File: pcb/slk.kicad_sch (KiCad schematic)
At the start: 10 parts, among them J1 Screw Terminal, P1 Power, P2 Analog, P3 Digital 1, P4 Digital 2, U1 MCP2515-xSO, Y1 Crystal

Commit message: finished schema
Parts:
- added U2: TJA1055T1, symbol Symbols:TJA1055T
- C1, C2: value C -> 22pF
- R1: value R -> 10K
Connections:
- net 5V: now also U2.10 (VCC)
- net GND: now also U2.13 (GND)
- net BAT+: now reaches J1.1 (Pin_1)
- net BAT+: now also U2.14 (BAT)
- net CANL: now reaches J1.2 (Pin_2)
- net CANL: now also U2.12 (CANL)
- net CANH: now reaches J1.3 (Pin_3)
- net CANH: now also U2.11 (CANH)
- net TX: now reaches U1.1 (TXCAN)
- net TX: now also U2.2 (TXD)
- net RX: now reaches U1.2 (RXCAN)
- net RX: now also U2.3 (RXD)
- new net EN: U2.6 (EN)
- new net ERR: U2.4 (ERR)
- new net INH: U2.1 (INH)
- new net STB: U2.5 (STB)
- new net WAKE: U2.7 (WAKE)
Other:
- moved on the sheet: J1

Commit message: add footprints
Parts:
- C1, C2: footprint (none) -> Capacitor_SMD:C_0402_1005Metric
- J1: footprint (none) -> TerminalBlock:TerminalBlock_bornier-3_P5.08mm
- P1, P3: footprint (none) -> Connector_PinHeader_2.54mm:PinHeader_1x08_P2.54mm_Vertical
- P2: footprint (none) -> Connector_PinHeader_2.54mm:PinHeader_1x06_P2.54mm_Vertical
- P4: footprint (none) -> Connector_PinHeader_2.54mm:PinHeader_1x10_P2.54mm_Vertical
- R1: footprint (none) -> Resistor_SMD:R_0402_1005Metric
- U2: footprint (none) -> Package_SO:SOIC-14_3.9x8.7mm_P1.27mm
- Y1: footprint (none) -> Crystal:Crystal_SMD_ECS_CSM3X-2Pin_7.6x4.1mm
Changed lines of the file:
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@@
 			)
 		)
-		(property "Footprint" ""
+		(property "Footprint" "Resistor_SMD:R_0402_1005Metric"
 			(at 139.7 122.428 90)
 			(effects
@@
 			)
 		)
-		(property "Footprint" ""
+		(property "Footprint" "TerminalBlock:TerminalBlock_bornier-3_P5.08mm"
 			(at 219.71 95.25 0)
 			(effects
@@
 			)
 		)
-		(property "Footprint" ""
+		(property "Footprint" "Connector_PinHeader_2.54mm:PinHeader_1x08_P2.54mm_Vertical"
 			(at 31.75 33.02 0)
 			(effects
@@
 			)
 		)
-		(property "Footprint" ""
+		(property "Footprint" "Connector_PinHeader_2.54mm:PinHeader_1x06_P2.54mm_Vertical"
 			(at 31.75 58.42 0)
 			(effects
@@
 			)
 		)
-		(property "Footprint" ""
+		(property "Footprint" "Connector_PinHeader_2.54mm:PinHeader_1x10_P2.54mm_Vertical"
 			(at 49.53 38.1 0)
 			(effects
@@
 			)
 		)
-		(property "Footprint" ""
+		(property "Footprint" "Capacitor_SMD:C_0402_1005Metric"
 			(at 94.9452 147.32 0)
 			(effects
@@
 			)
 		)
-		(property "Footprint" ""
+		(property "Footprint" "Crystal:Crystal_SMD_ECS_CSM3X-2Pin_7.6x4.1mm"
 			(at 90.17 134.62 0)
 			(effects
@@
 			)
 		)
-		(property "Footprint" ""
+		(property "Footprint" "Capacitor_SMD:C_0402_1005Metric"
 			(at 87.3252 147.32 0)
 			(effects
@@
 			)
 		)
-		(property "Footprint" ""
+		(property "Footprint" "Connector_PinHeader_2.54mm:PinHeader_1x08_P2.54mm_Vertical"
 			(at 49.53 63.5 0)
 			(effects
@@
 			)
 		)
-		(property "Footprint" ""
+		(property "Footprint" "Package_SO:SOIC-14_3.9x8.7mm_P1.27mm"
 			(at 162.56 87.63 0)
 			(effects

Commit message: draw board outline
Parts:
- added H1, H2, H3, H4: MountingHole, MountingHole:MountingHole_3.2mm_M3, symbol Mechanical:MountingHole

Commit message: it should work now
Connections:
- net EN: now also P3.7 (Pin_7)
- net ERR: now also P3.5 (Pin_5)
- net INH: now also P3.4 (Pin_4)
- net STB: now also P3.6 (Pin_6)
- net WAKE: now also P3.8 (Pin_8)
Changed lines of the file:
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@@
+	(wire
+		(pts
+			(xy 58.42 63.5) (xy 54.61 63.5)
+		)
+		(stroke
+			(width 0)
+			(type default)
+		)
+	)
+	(wire
+		(pts
+			(xy 58.42 58.42) (xy 54.61 58.42)
+		)
+		(stroke
+			(width 0)
+			(type default)
+		)
+	)
 	(wire
 		(pts
@@
 	(wire
 		(pts
+			(xy 58.42 55.88) (xy 54.61 55.88)
+		)
+		(stroke
+			(width 0)
+			(type default)
+		)
+	)
+	(wire
+		(pts
 			(xy 187.96 97.79) (xy 214.63 97.79)
 		)
@@
 	(wire
 		(pts
+			(xy 58.42 60.96) (xy 54.61 60.96)
+		)
+		(stroke
+			(width 0)
+			(type default)
+		)
+	)
+	(wire
+		(pts
 			(xy 190.5 92.71) (xy 187.96 92.71)
 		)
@@
 		(pts
 			(xy 116.84 81.28) (xy 116.84 85.09)
+		)
+		(stroke
+			(width 0)
+			(type default)
+		)
+	)
+	(wire
+		(pts
+			(xy 58.42 53.34) (xy 54.61 53.34)
 		)
 		(stroke
@@
 		)
 	)
+	(label "ERR"
+		(at 58.42 60.96 0)
+		(fields_autoplaced yes)
+		(effects
+			(font
+				(size 1.27 1.27)
+			)
+			(justify left bottom)
+		)
+	)
 	(label "CS"
 		(at 58.42 43.18 0)
@@
 		)
 	)
+	(label "INH"
+		(at 58.42 63.5 0)
+		(fields_autoplaced yes)
+		(effects
+			(font
+				(size 1.27 1.27)
+			)
+			(justify left bottom)
+		)
+	)
 	(label "SCK"
 		(at 58.42 35.56 0)
@@
 		)
 	)
+	(label "WAKE"
+		(at 58.42 53.34 0)
+		(fields_autoplaced yes)
+		(effects
+			(font
+				(size 1.27 1.27)
+			)
+			(justify left bottom)
+		)
+	)
 	(label "SCK"
 		(at 96.52 97.79 0)
@@
 		)
 	)
+	(label "STB"
+		(at 58.42 58.42 0)
+		(fields_autoplaced yes)
+		(effects
+			(font
+				(size 1.27 1.27)
+			)
+			(justify left bottom)
+		)
+	)
 	(label "CANL"
 		(at 190.5 95.25 0)
@@
 		(fields_autoplaced yes)
 		(effects
+			(font
+				(size 1.27 1.27)
+			)
+			(justify left bottom)
+		)
+	)
+	(label "EN"
+		(at 58.42 55.88 0)
+		(fields_autoplaced yes)
+		(effects

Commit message: leds
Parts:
- added D1: ERR, LED_SMD:LED_0603_1608Metric, symbol Device:LED
- added D2: RX, LED_SMD:LED_0603_1608Metric, symbol Device:LED
- added D3: TX, LED_SMD:LED_0603_1608Metric, symbol Device:LED
- added R1, R2, R3: R, Resistor_SMD:R_0402_1005Metric, symbol Device:R
- added SW1: SW_SPDT, Button_Switch_SMD:SW_SPDT_CK_JS102011SAQN, symbol Switch:SW_SPDT
- Y1: value Crystal -> 16MHz
- renumbered R1 to R4
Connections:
- net 5V: now also R1.2, SW1.3 (C)
- net BAT+: now also J1.3 (Pin_3), SW1.1 (A); no longer J1.1 (Pin_1), U2.14 (BAT)
- net CANH: now also J1.1 (Pin_1); no longer J1.3 (Pin_3)
- net ERR: now also D1.1 (K)
- net GND: now also D2.1 (K), D3.1 (K)
- net RX: now also R2.2
- net TX: now also R3.2
- new net: D3.2 (A), R3.1
- new net: D2.2 (A), R2.1
- new net: D1.2 (A), R1.1
- new net: SW1.2 (B), U2.14 (BAT)

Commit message: done
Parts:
- C1, C2: Part Number (none) -> GRM1555C1H220JA01D
- D1: Part Number (none) -> LTST-C190GKT
- D2: Part Number (none) -> LTST-C191KRKT
- D3: Part Number (none) -> LTST-C193TBKT-5A
- J1: Part Number (none) -> TERM BLK 3P SIDE ENT 5.08MM PCB
- P1, P3: Part Number (none) -> 200-SSW10803GS
- P2: Part Number (none) -> 200-SSW10603GS
- P4: Part Number (none) -> 200-SSW11003GS
- R1, R2, R3: value R -> 330; Part Number (none) -> RC0402JR-07330RL
- R4: Part Number (none) -> RC0402JR-0710KL
- SW1: Part Number (none) -> JS102011SAQN
- U1: Part Number (none) -> MCP2515T-I/SO
- U2: Part Number (none) -> TJA1055T/1J (935302723118)
- Y1: Part Number (none) -> ECS-160-20-3X-TR
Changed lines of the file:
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@@
+			)
+		)
+		(property "Part Number" "RC0402JR-0710KL"
+			(at 139.7 120.65 0)
+			(effects
+				(font
+					(size 1.27 1.27)
+				)
+				(hide yes)
 			)
 		)
@@
 			)
 		)
+		(property "Part Number" "TERM BLK 3P SIDE ENT 5.08MM PCB"
+			(at 219.71 95.25 0)
+			(effects
+				(font
+					(size 1.27 1.27)
+				)
+				(hide yes)
+			)
+		)
 		(pin "2"
 		)
@@
 			)
 		)
+		(property "Part Number" "200-SSW10803GS"
+			(at 31.75 33.02 0)
+			(effects
+				(font
+					(size 1.27 1.27)
+				)
+				(hide yes)
+			)
+		)
 		(pin "1"
 		)
@@
 			)
 		)
+		(property "Part Number" ""
+			(at 127 25.4 0)
+			(effects
+				(font
+					(size 1.27 1.27)
+				)
+				(hide yes)
+			)
+		)
 		(instances
 			(project "slk"
@@
 		)
 		(property "Description" "Light emitting diode"
+			(at 173.99 149.86 0)
+			(effects
+				(font
+					(size 1.27 1.27)
+				)
+				(hide yes)
+			)
+		)
+		(property "Part Number" "LTST-C193TBKT-5A"
 			(at 173.99 149.86 0)
 			(effects
@@
 			)
 		)
+		(property "Part Number" "200-SSW10603GS"
+			(at 31.75 58.42 0)
+			(effects
+				(font
+					(size 1.27 1.27)
+				)
+				(hide yes)
+			)
+		)
 		(pin "1"
 		)
@@
 			)
 		)
+		(property "Part Number" "200-SSW11003GS"
+			(at 49.53 38.1 0)
+			(effects
+				(font
+					(size 1.27 1.27)
+				)
+				(hide yes)
+			)
+		)
 		(pin "4"
 		)
@@
 			)
 		)
+		(property "Part Number" "GRM1555C1H220JA01D"
+			(at 93.98 143.51 0)
+			(effects
+				(font
+					(size 1.27 1.27)
+				)
+				(hide yes)
+			)
+		)
 		(pin "2"
 		)
@@
 			)
 		)
-		(property "Value" "R"
+		(property "Value" "330"
 			(at 181.6735 137.668 90)
 			(effects
@@
 		)
 		(property "Description" "Resistor"
+			(at 181.61 140.97 0)
+			(effects
+				(font
+					(size 1.27 1.27)
+				)
+				(hide yes)
+			)
+		)
+		(property "Part Number" "RC0402JR-07330RL"
 			(at 181.61 140.97 0)
 			(effects
@@
 			)
 		)
+		(property "Part Number" "MCP2515T-I/SO"
+			(at 116.84 105.41 0)
+			(effects
+				(font
+					(size 1.27 1.27)
+				)
+				(hide yes)
+			)
+		)
 		(pin "18"
 		)
@@
 		)
 		(property "Description" "Light emitting diode"
+			(at 173.99 130.81 0)
+			(effects
+				(font
+					(size 1.27 1.27)
+				)
+				(hide yes)
+			)
+		)
+		(property "Part Number" "LTST-C190GKT "
 			(at 173.99 130.81 0)
 			(effects
@@
 			)
 		)
+		(property "Part Number" "ECS-160-20-3X-TR"
+			(at 90.17 134.62 0)
+			(effects
+				(font
+					(size 1.27 1.27)
+				)
+				(hide yes)
+			)
+		)
 		(pin "2"
 		)
@@
 		)
 		(property "Description" "Unpolarized capacitor"
+			(at 86.36 143.51 0)
+			(effects
+				(font
+					(size 1.27 1.27)
+				)
+				(hide yes)
+			)
+		)
+		(property "Part Number" "GRM1555C1H220JA01D"
 			(at 86.36 143.51 0)
 			(effects
@@
 			)
 		)
+		(property "Part Number" ""
+			(at 127 38.1 0)
+			(effects
+				(font
+					(size 1.27 1.27)
+				)
+				(hide yes)
+			)
+		)
 		(instances
 			(project "slk"
@@
 			)
 		)
-		(property "Value" "R"
+		(property "Value" "330"
 			(at 181.6735 147.066 90)
 			(effects
@@
 		)
 		(property "Description" "Resistor"
+			(at 181.61 149.86 0)
+			(effects
+				(font
+					(size 1.27 1.27)
+				)
+				(hide yes)
+			)
+		)
+		(property "Part Number" "RC0402JR-07330RL"
 			(at 181.61 149.86 0)
 			(effects
@@
 			)
 		)
+		(property "Part Number" ""
+			(at 127 44.45 0)
+			(effects
+				(font
+					(size 1.27 1.27)
+				)
+				(hide yes)
+			)
+		)
 		(instances
 			(project "slk"
@@
 			)
 		)
+		(property "Part Number" "JS102011SAQN"
+			(at 205.74 83.82 0)
+			(effects
+				(font
+					(size 1.27 1.27)
+				)
+				(hide yes)
+			)
+		)
 		(pin "2"
 		)
@@
 		)
 		(property "Description" "Light emitting diode"
+			(at 173.99 140.97 0)
+			(effects
+				(font
+					(size 1.27 1.27)
+				)
+				(hide yes)
+			)
+		)
+		(property "Part Number" "LTST-C191KRKT"
 			(at 173.99 140.97 0)
 			(effects
@@
 			)
 		)
+		(property "Part Number" "200-SSW10803GS"
+			(at 49.53 63.5 0)
+			(effects
+				(font
+					(size 1.27 1.27)
+				)
+				(hide yes)
+			)
+		)
 		(pin "2"
 		)
@@
 			)
 		)
-		(property "Value" "R"
+		(property "Value" "330"
 			(at 181.6735 127.508 90)
 			(effects
@@
 		)
 		(property "Description" "Resistor"
+			(at 181.61 130.81 0)
+			(effects
+				(font
+					(size 1.27 1.27)
+				)
+				(hide yes)
+			)
+		)
+		(property "Part Number" "RC0402JR-07330RL"
 			(at 181.61 130.81 0)
 			(effects
@@
 			)
 		)
+		(property "Part Number" ""
+			(at 127 31.75 0)
+			(effects
+				(font
+					(size 1.27 1.27)
+				)
+				(hide yes)
+			)
+		)
 		(instances
 			(project "slk"
@@
 			(at 162.56 87.63 0)
 			(effects
+				(font
+					(size 1.27 1.27)
+				)
+				(hide yes)
+			)
+		)
+		(property "Part Number" "TJA1055T/1J (935302723118) "
+			(at 162.56 87.63 0)
+			(effects

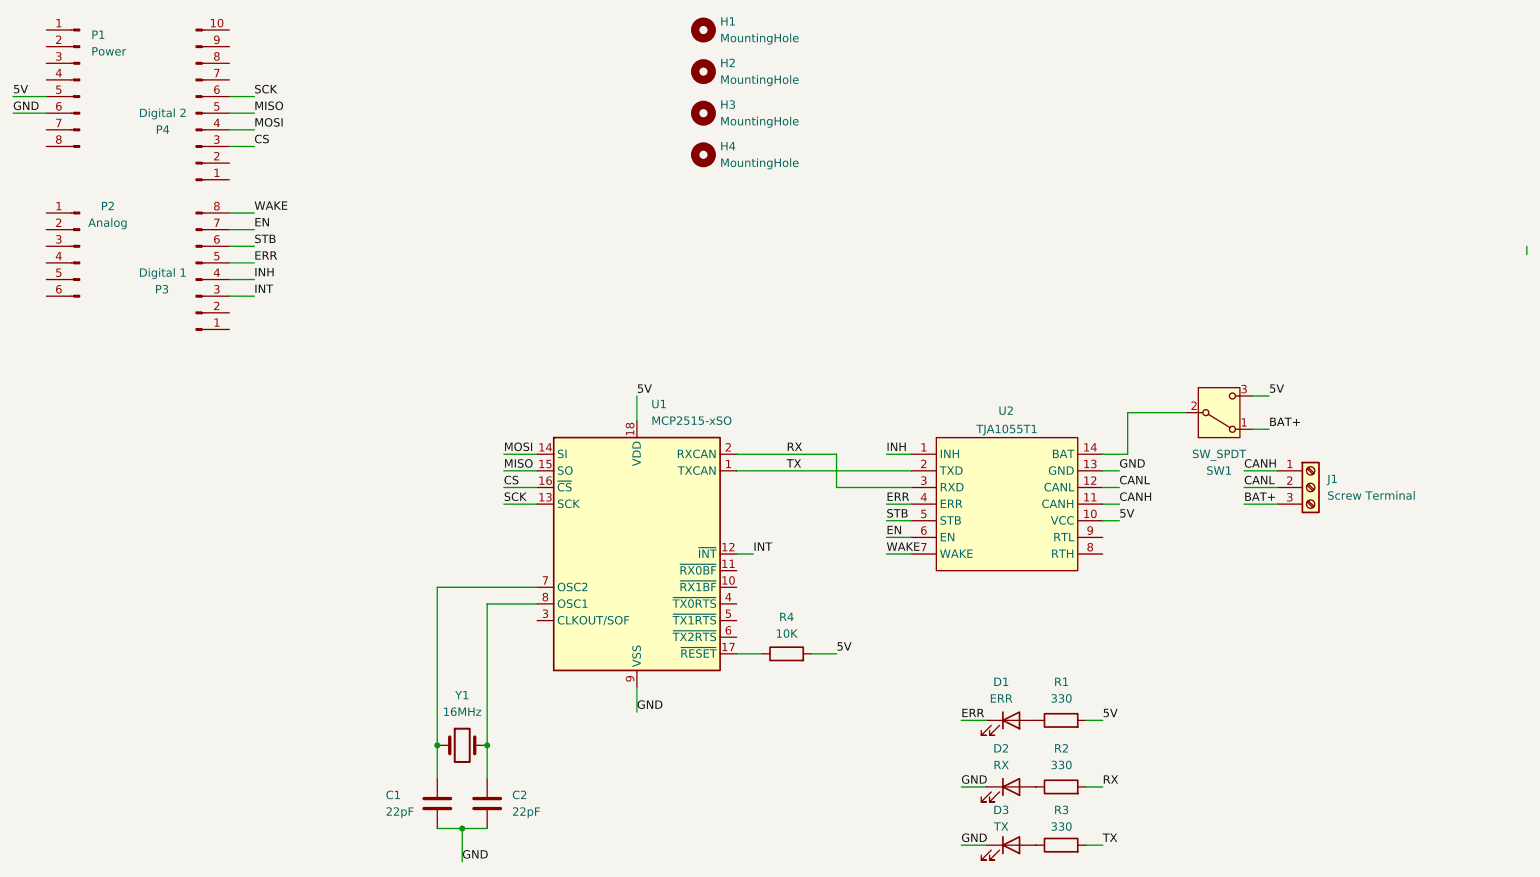
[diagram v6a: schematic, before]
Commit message: add manual resistors
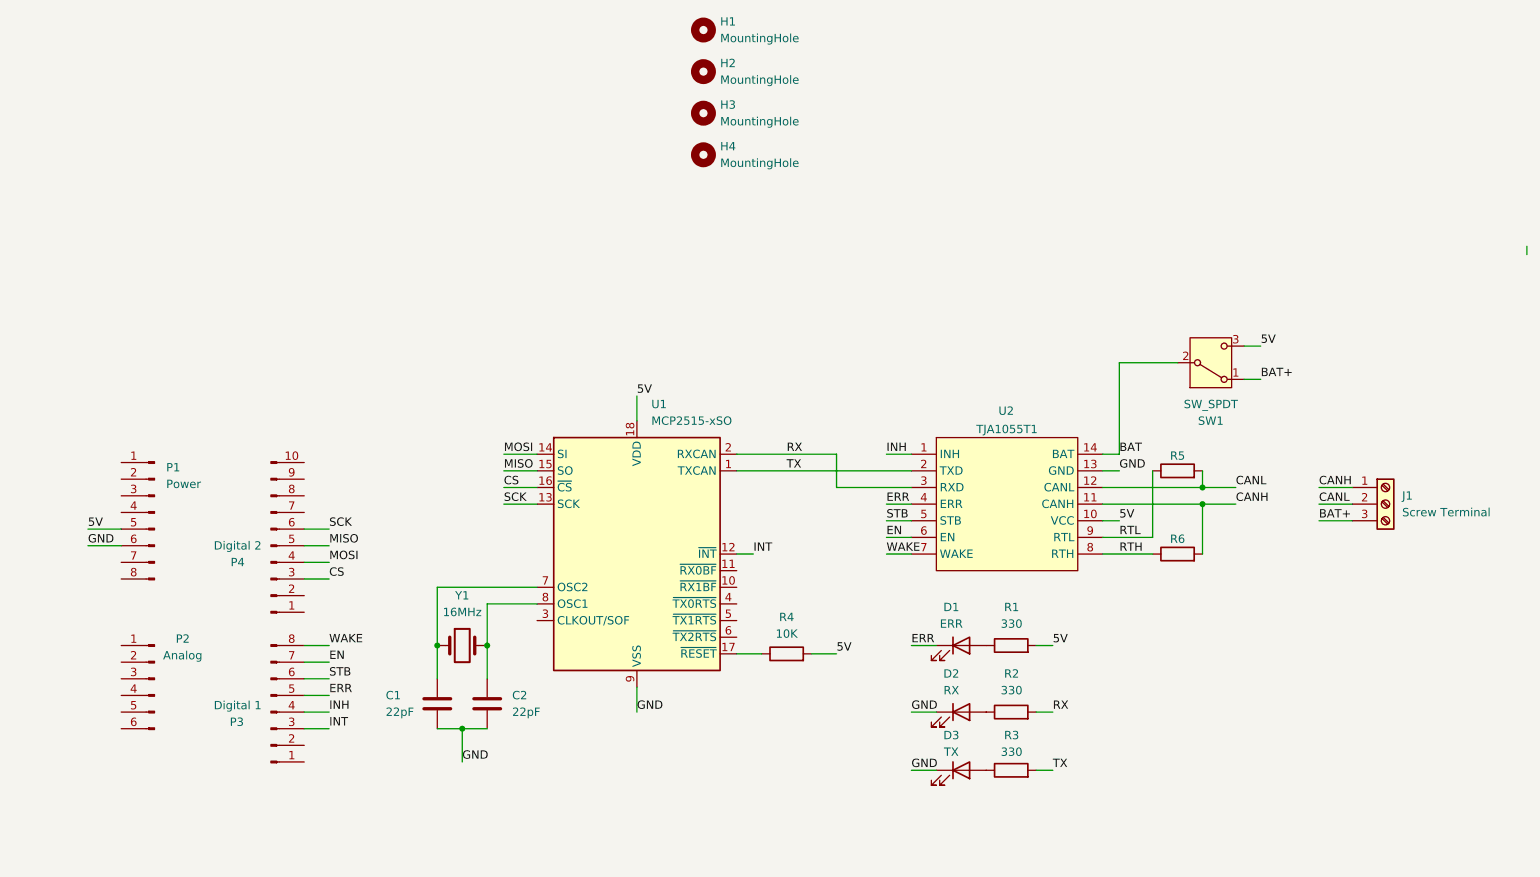
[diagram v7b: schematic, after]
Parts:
- added R5, R6: R, Resistor_THT:R_Axial_DIN0207_L6.3mm_D2.5mm_P7.62mm_Horizontal, symbol Device:R
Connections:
- net CANH: now also R6.2
- net CANL: now also R5.2
- net BAT: now reaches SW1.2 (B), U2.14 (BAT)
- net RTH: now reaches U2.8 (RTH)
- net RTH: now also R6.1
- net RTL: now reaches U2.9 (RTL)
- net RTL: now also R5.1
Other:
- moved on the sheet: C1, C2, D1, D2, D3, J1, P1, P2, P3, P4, R1, R2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
